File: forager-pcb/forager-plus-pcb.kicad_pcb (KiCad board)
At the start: 2 copper layers, 114.6 x 96.3 mm, 26 parts, among them J2 Conn_01x02_Pin, U1 XIAO nRF52840 Plus

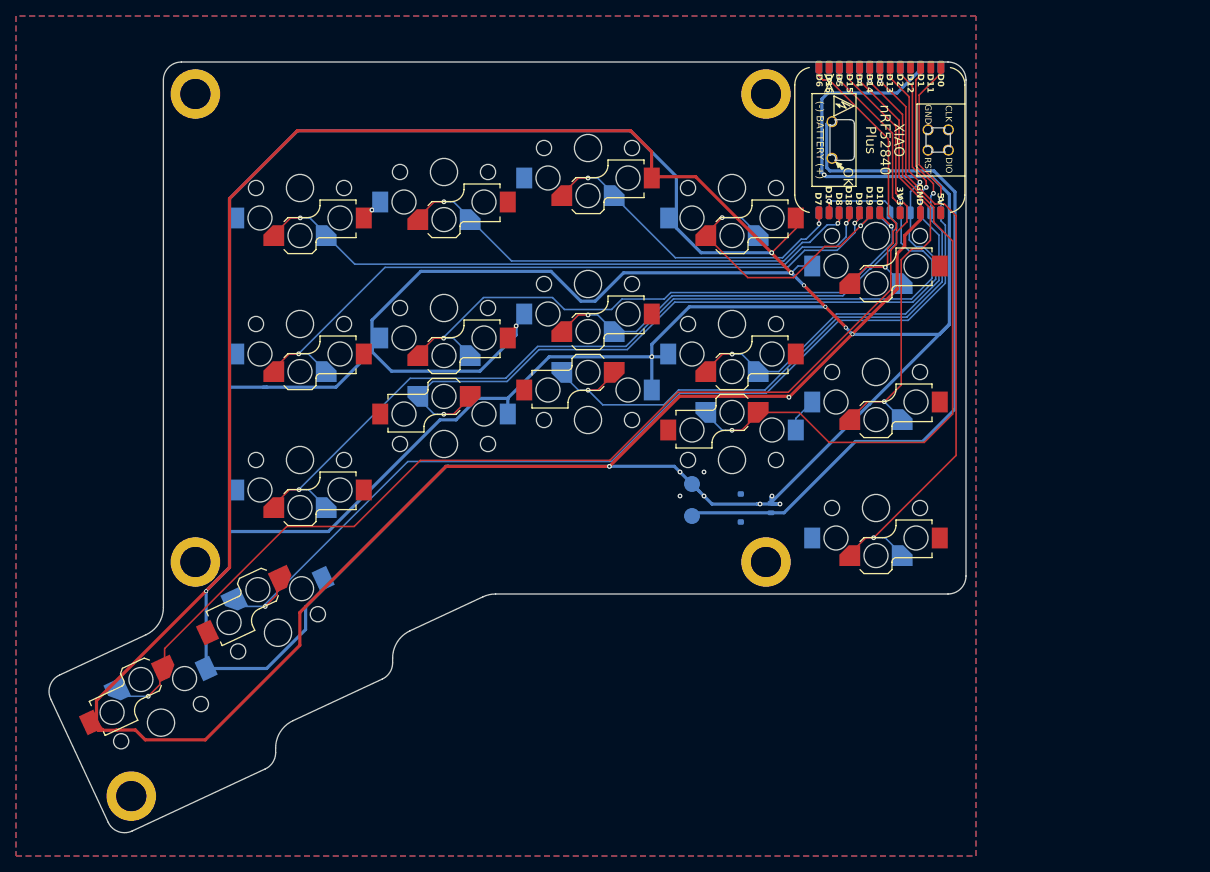
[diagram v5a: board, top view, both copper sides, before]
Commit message: Improve front/back balance; keep power on edge (for switch?)
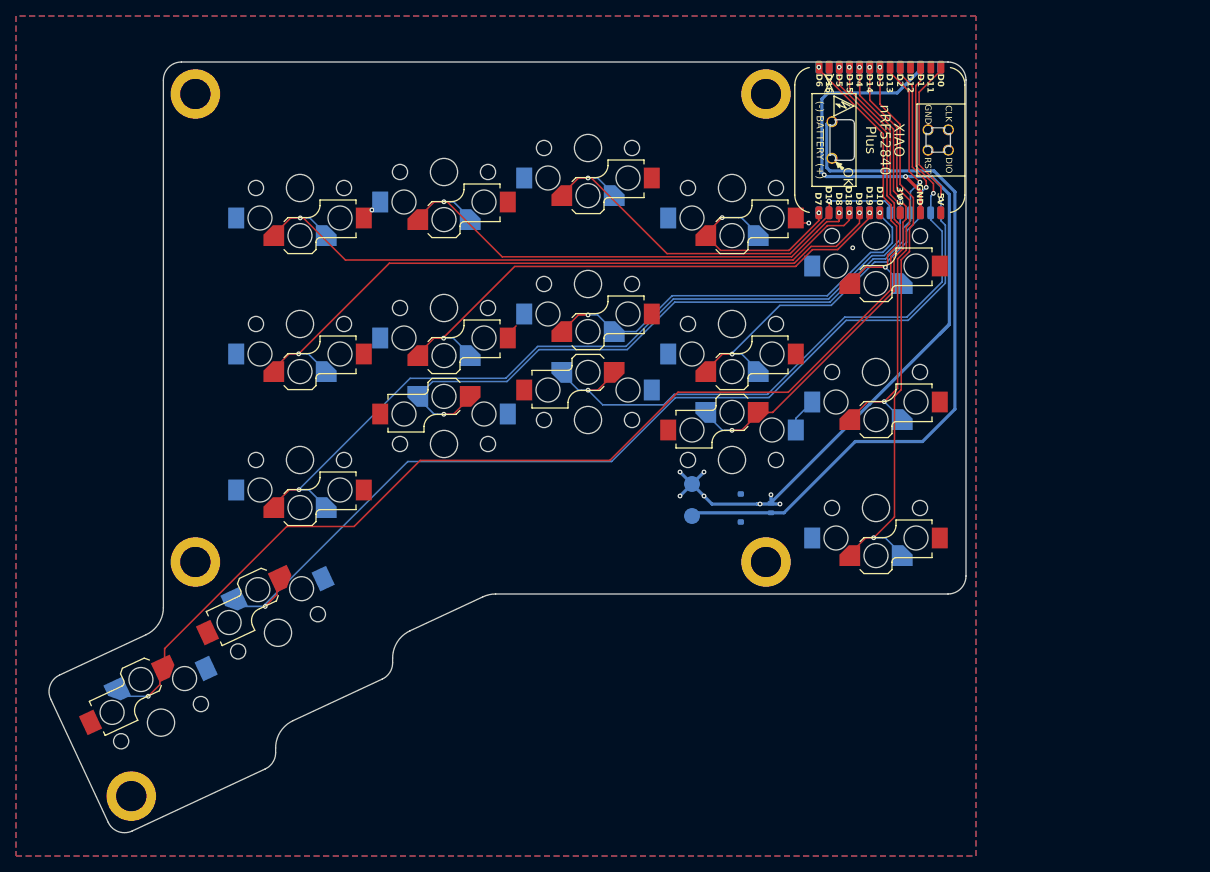
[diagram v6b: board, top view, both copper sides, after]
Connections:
- U1 pad B:D13: RM2 -> RT2
- U1 pad B:D14: RT3 -> RM1
- U1 pad B:D18: (no net) -> RB3
- U1 pad B:D19: RB3 -> RM4
- U1 pad B:D3: RM1 -> RM2
- U1 pad B:D6: RT2 -> RT3
- U1 pad B:D9: RM4 -> RB0
- U1 pad F:D10: RM1 -> RM2
- U1 pad F:D14: RB3 -> RM4
- U1 pad F:D15: RB0 -> RB3
- U1 pad F:D17: RM2 -> RT2
- U1 pad F:D19: RT3 -> RM1
- U1 pad F:D4: RM4 -> RB0
- U1 pad F:D7: RT2 -> RT3
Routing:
- net GND: track 853.9 -> 122.2 mm, vias 20 -> 12
- net RB3: track 84.9 -> 62.8 mm
- net RT2: track 41.7 -> 54.5 mm
- net RM2: track 61.9 -> 51.8 mm
- net RT3: track 35.7 -> 25.7 mm
- net RB0: track 129.4 -> 120.0 mm, vias 2 -> 3
- net RB1: track 109.6 -> 100.5 mm
- net RM1: track 76.9 -> 67.8 mm
- net RB4: track 77.7 -> 70.7 mm
- net RM4: track 58.7 -> 53.4 mm
- net RM3: track 64.6 -> 59.7 mm
- net RT4: track 40.9 -> 37.6 mm
- net RT1: track 61.1 -> 63.4 mm
- net RH0: track 151.4 -> 149.8 mm
- net RT0: track 80.8 -> 82.1 mm
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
